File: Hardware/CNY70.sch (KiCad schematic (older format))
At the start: 3 parts

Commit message: Battery charger IC added
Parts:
- gave numbers to parts that had none: 3
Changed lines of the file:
@@
 Connection ~ 6250 4150
 $Comp
-L Sensor_Proximity:CNY70 U?
+L Sensor_Proximity:CNY70 U4
 U 1 1 5FEE7D3D
 P 5900 4050
-F 0 "U?" H 5900 4367 50  0000 C CNN
+AR Path="/5FEE7C2C/5FEE7D3D" Ref="U4"  Part="1"
+AR Path="/5FEFD023/5FEE7D3D" Ref="U7"  Part="1"
+F 0 "U7" H 5900 4367 50  0000 C CNN
 F 1 "CNY70" H 5900 4276 50  0000 C CNN
 F 2 "OptoDevice:Vishay_CNY70" H 5900 3850 50  0001 C CNN
@@
 $EndComp
 $Comp
-L Device:R_Small_US R?
+L Device:R_Small_US R19
 U 1 1 5FEE87CE
 P 5550 4300
-F 0 "R?" H 5618 4346 50  0000 L CNN
+AR Path="/5FEE7C2C/5FEE87CE" Ref="R19"  Part="1"
+AR Path="/5FEFD023/5FEE87CE" Ref="R21"  Part="1"
+F 0 "R21" H 5618 4346 50  0000 L CNN
 F 1 "80" H 5618 4255 50  0000 L CNN
 F 2 "" H 5550 4300 50  0001 C CNN
@@
 $EndComp
 $Comp
-L power:GND #PWR?
+L power:GND #PWR039
 U 1 1 5FEE941E
 P 5550 4400
-F 0 "#PWR?" H 5550 4150 50  0001 C CNN
+AR Path="/5FEE7C2C/5FEE941E" Ref="#PWR039"  Part="1"
+AR Path="/5FEFD023/5FEE941E" Ref="#PWR043"  Part="1"
+F 0 "#PWR043" H 5550 4150 50  0001 C CNN
 F 1 "GND" H 5555 4227 50  0000 C CNN
 F 2 "" H 5550 4400 50  0001 C CNN
@@
 $EndComp
 $Comp
-L power:+3.3V #PWR?
+L power:+3.3V #PWR037
 U 1 1 5FEFD560
 P 5550 3900
-F 0 "#PWR?" H 5550 3750 50  0001 C CNN
+AR Path="/5FEE7C2C/5FEFD560" Ref="#PWR037"  Part="1"
+AR Path="/5FEFD023/5FEFD560" Ref="#PWR041"  Part="1"
+F 0 "#PWR041" H 5550 3750 50  0001 C CNN
 F 1 "+3.3V" H 5565 4073 50  0000 C CNN
 F 2 "" H 5550 3900 50  0001 C CNN
@@
 $EndComp
 $Comp
-L power:+3.3V #PWR?
+L power:+3.3V #PWR038
 U 1 1 5FEFD561
 P 6250 3900
-F 0 "#PWR?" H 6250 3750 50  0001 C CNN
+AR Path="/5FEE7C2C/5FEFD561" Ref="#PWR038"  Part="1"
+AR Path="/5FEFD023/5FEFD561" Ref="#PWR042"  Part="1"
+F 0 "#PWR042" H 6250 3750 50  0001 C CNN
 F 1 "+3.3V" H 6265 4073 50  0000 C CNN
 F 2 "" H 6250 3900 50  0001 C CNN
@@
 $EndComp
 $Comp
-L Device:R_Small_US R?
+L Device:R_Small_US R20
 U 1 1 5FEFD562
 P 6250 4300
-F 0 "R?" H 6318 4346 50  0000 L CNN
+AR Path="/5FEE7C2C/5FEFD562" Ref="R20"  Part="1"
+AR Path="/5FEFD023/5FEFD562" Ref="R22"  Part="1"
+F 0 "R22" H 6318 4346 50  0000 L CNN
 F 1 "1k" H 6318 4255 50  0000 L CNN
 F 2 "" H 6250 4300 50  0001 C CNN
@@
 $EndComp
 $Comp
-L power:GND #PWR?
+L power:GND #PWR040
 U 1 1 5FEFD563
 P 6250 4400
-F 0 "#PWR?" H 6250 4150 50  0001 C CNN
+AR Path="/5FEE7C2C/5FEFD563" Ref="#PWR040"  Part="1"
+AR Path="/5FEFD023/5FEFD563" Ref="#PWR044"  Part="1"
+F 0 "#PWR044" H 6250 4150 50  0001 C CNN
 F 1 "GND" H 6255 4227 50  0000 C CNN
 F 2 "" H 6250 4400 50  0001 C CNN

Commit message: Replaced ESP-WROOM-32D with ESP32-CAM
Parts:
- added R?: 80, symbol Device:R_Small_US
- renumbered R20 to R10, R19 to R9, U4 to U3
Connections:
- net +3V3: now also R?.1; no longer U3.3 (C)
- new net: R?.2, U3.3 (C)
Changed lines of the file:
@@
 	5550 3950 5600 3950
 Wire Wire Line
-	6250 3900 6250 3950
+	6250 3700 6250 3750
 Wire Wire Line
 	6250 3950 6200 3950
@@
 Connection ~ 6250 4150
 $Comp
-L Sensor_Proximity:CNY70 U4
+L Sensor_Proximity:CNY70 U3
 U 1 1 5FEE7D3D
 P 5900 4050
-AR Path="/5FEE7C2C/5FEE7D3D" Ref="U4"  Part="1"
-AR Path="/5FEFD023/5FEE7D3D" Ref="U7"  Part="1"
-F 0 "U7" H 5900 4367 50  0000 C CNN
+AR Path="/5FEE7C2C/5FEE7D3D" Ref="U3"  Part="1"
+AR Path="/5FEFD023/5FEE7D3D" Ref="U4"  Part="1"
+F 0 "U3" H 5900 4367 50  0000 C CNN
 F 1 "CNY70" H 5900 4276 50  0000 C CNN
 F 2 "OptoDevice:Vishay_CNY70" H 5900 3850 50  0001 C CNN
@@
 $EndComp
 $Comp
-L Device:R_Small_US R19
+L Device:R_Small_US R9
 U 1 1 5FEE87CE
 P 5550 4300
-AR Path="/5FEE7C2C/5FEE87CE" Ref="R19"  Part="1"
-AR Path="/5FEFD023/5FEE87CE" Ref="R21"  Part="1"
-F 0 "R21" H 5618 4346 50  0000 L CNN
+AR Path="/5FEE7C2C/5FEE87CE" Ref="R9"  Part="1"
+AR Path="/5FEFD023/5FEE87CE" Ref="R11"  Part="1"
+F 0 "R9" H 5618 4346 50  0000 L CNN
 F 1 "80" H 5618 4255 50  0000 L CNN
 F 2 "" H 5550 4300 50  0001 C CNN
@@
 $EndComp
 $Comp
-L power:GND #PWR039
+L power:GND #PWR028
 U 1 1 5FEE941E
 P 5550 4400
-AR Path="/5FEE7C2C/5FEE941E" Ref="#PWR039"  Part="1"
-AR Path="/5FEFD023/5FEE941E" Ref="#PWR043"  Part="1"
-F 0 "#PWR043" H 5550 4150 50  0001 C CNN
+AR Path="/5FEE7C2C/5FEE941E" Ref="#PWR028"  Part="1"
+AR Path="/5FEFD023/5FEE941E" Ref="#PWR032"  Part="1"
+F 0 "#PWR028" H 5550 4150 50  0001 C CNN
 F 1 "GND" H 5555 4227 50  0000 C CNN
 F 2 "" H 5550 4400 50  0001 C CNN
@@
 $EndComp
 $Comp
-L power:+3.3V #PWR037
+L power:+3.3V #PWR026
 U 1 1 5FEFD560
 P 5550 3900
-AR Path="/5FEE7C2C/5FEFD560" Ref="#PWR037"  Part="1"
-AR Path="/5FEFD023/5FEFD560" Ref="#PWR041"  Part="1"
-F 0 "#PWR041" H 5550 3750 50  0001 C CNN
+AR Path="/5FEE7C2C/5FEFD560" Ref="#PWR026"  Part="1"
+AR Path="/5FEFD023/5FEFD560" Ref="#PWR030"  Part="1"
+F 0 "#PWR026" H 5550 3750 50  0001 C CNN
 F 1 "+3.3V" H 5565 4073 50  0000 C CNN
 F 2 "" H 5550 3900 50  0001 C CNN
@@
 $EndComp
 $Comp
-L power:+3.3V #PWR038
+L power:+3.3V #PWR027
 U 1 1 5FEFD561
-P 6250 3900
-AR Path="/5FEE7C2C/5FEFD561" Ref="#PWR038"  Part="1"
-AR Path="/5FEFD023/5FEFD561" Ref="#PWR042"  Part="1"
-F 0 "#PWR042" H 6250 3750 50  0001 C CNN
-F 1 "+3.3V" H 6265 4073 50  0000 C CNN
-F 2 "" H 6250 3900 50  0001 C CNN
-F 3 "" H 6250 3900 50  0001 C CNN
-	1    6250 3900
+P 6250 3700
+AR Path="/5FEE7C2C/5FEFD561" Ref="#PWR027"  Part="1"
+AR Path="/5FEFD023/5FEFD561" Ref="#PWR031"  Part="1"
+F 0 "#PWR027" H 6250 3550 50  0001 C CNN
+F 1 "+3.3V" H 6265 3873 50  0000 C CNN
+F 2 "" H 6250 3700 50  0001 C CNN
+F 3 "" H 6250 3700 50  0001 C CNN
+	1    6250 3700
 	1    0    0    -1
 $EndComp
 $Comp
-L Device:R_Small_US R20
+L Device:R_Small_US R10
 U 1 1 5FEFD562
 P 6250 4300
-AR Path="/5FEE7C2C/5FEFD562" Ref="R20"  Part="1"
-AR Path="/5FEFD023/5FEFD562" Ref="R22"  Part="1"
-F 0 "R22" H 6318 4346 50  0000 L CNN
+AR Path="/5FEE7C2C/5FEFD562" Ref="R10"  Part="1"
+AR Path="/5FEFD023/5FEFD562" Ref="R12"  Part="1"
+F 0 "R10" H 6318 4346 50  0000 L CNN
 F 1 "1k" H 6318 4255 50  0000 L CNN
 F 2 "" H 6250 4300 50  0001 C CNN
@@
 $EndComp
 $Comp
-L power:GND #PWR040
+L power:GND #PWR029
 U 1 1 5FEFD563
 P 6250 4400
-AR Path="/5FEE7C2C/5FEFD563" Ref="#PWR040"  Part="1"
-AR Path="/5FEFD023/5FEFD563" Ref="#PWR044"  Part="1"
-F 0 "#PWR044" H 6250 4150 50  0001 C CNN
+AR Path="/5FEE7C2C/5FEFD563" Ref="#PWR029"  Part="1"
+AR Path="/5FEFD023/5FEFD563" Ref="#PWR033"  Part="1"
+F 0 "#PWR029" H 6250 4150 50  0001 C CNN
 F 1 "GND" H 6255 4227 50  0000 C CNN
 F 2 "" H 6250 4400 50  0001 C CNN
@@
 Text HLabel 6300 4150 2    50   Output ~ 0
 IR
+$Comp
+L Device:R_Small_US R?
+U 1 1 5FF4EFE4
+P 6250 3850
+AR Path="/5FEE7C2C/5FF4EFE4" Ref="R?"  Part="1"
+AR Path="/5FEFD023/5FF4EFE4" Ref="R?"  Part="1"
+F 0 "R?" H 6318 3896 50  0000 L CNN
+F 1 "80" H 6318 3805 50  0000 L CNN
+F 2 "" H 6250 3850 50  0001 C CNN
+F 3 "~" H 6250 3850 50  0001 C CNN
+	1    6250 3850
+	1    0    0    -1
+$EndComp
 $EndSCHEMATC

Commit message: Signed-off-by: Usman <usmanmehmood55@gmail.com>
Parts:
- removed R?: 80, symbol Device:R_Small_US
- added R9: 80, symbol Device:R_Small_US
- renumbered R9 to R10, R10 to R11
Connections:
- net +3V3: now also U3.3 (C)
- net IR: now also R9.2; no longer R11.1, U3.4 (E)
- new net: R11.1, R9.1, U3.4 (E)
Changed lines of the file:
@@
 	5550 3950 5600 3950
 Wire Wire Line
-	6250 3700 6250 3750
+	6250 3900 6250 3950
 Wire Wire Line
 	6250 3950 6200 3950
@@
 $EndComp
 $Comp
-L Device:R_Small_US R9
+L Device:R_Small_US R10
 U 1 1 5FEE87CE
 P 5550 4300
-AR Path="/5FEE7C2C/5FEE87CE" Ref="R9"  Part="1"
-AR Path="/5FEFD023/5FEE87CE" Ref="R11"  Part="1"
-F 0 "R9" H 5618 4346 50  0000 L CNN
+AR Path="/5FEE7C2C/5FEE87CE" Ref="R10"  Part="1"
+AR Path="/5FEFD023/5FEE87CE" Ref="R13"  Part="1"
+F 0 "R10" H 5618 4346 50  0000 L CNN
 F 1 "80" H 5618 4255 50  0000 L CNN
 F 2 "" H 5550 4300 50  0001 C CNN
@@
 $EndComp
 $Comp
-L power:+3.3V #PWR026
+L power:+3.3V #PWR027
 U 1 1 5FEFD560
 P 5550 3900
-AR Path="/5FEE7C2C/5FEFD560" Ref="#PWR026"  Part="1"
-AR Path="/5FEFD023/5FEFD560" Ref="#PWR030"  Part="1"
-F 0 "#PWR026" H 5550 3750 50  0001 C CNN
+AR Path="/5FEE7C2C/5FEFD560" Ref="#PWR027"  Part="1"
+AR Path="/5FEFD023/5FEFD560" Ref="#PWR031"  Part="1"
+F 0 "#PWR027" H 5550 3750 50  0001 C CNN
 F 1 "+3.3V" H 5565 4073 50  0000 C CNN
 F 2 "" H 5550 3900 50  0001 C CNN
@@
 $EndComp
 $Comp
-L power:+3.3V #PWR027
+L power:+3.3V #PWR026
 U 1 1 5FEFD561
-P 6250 3700
-AR Path="/5FEE7C2C/5FEFD561" Ref="#PWR027"  Part="1"
-AR Path="/5FEFD023/5FEFD561" Ref="#PWR031"  Part="1"
-F 0 "#PWR027" H 6250 3550 50  0001 C CNN
-F 1 "+3.3V" H 6265 3873 50  0000 C CNN
-F 2 "" H 6250 3700 50  0001 C CNN
-F 3 "" H 6250 3700 50  0001 C CNN
-	1    6250 3700
+P 6250 3900
+AR Path="/5FEE7C2C/5FEFD561" Ref="#PWR026"  Part="1"
+AR Path="/5FEFD023/5FEFD561" Ref="#PWR030"  Part="1"
+F 0 "#PWR026" H 6250 3750 50  0001 C CNN
+F 1 "+3.3V" H 6265 4073 50  0000 C CNN
+F 2 "" H 6250 3900 50  0001 C CNN
+F 3 "" H 6250 3900 50  0001 C CNN
+	1    6250 3900
 	1    0    0    -1
 $EndComp
 $Comp
-L Device:R_Small_US R10
+L Device:R_Small_US R11
 U 1 1 5FEFD562
 P 6250 4300
-AR Path="/5FEE7C2C/5FEFD562" Ref="R10"  Part="1"
-AR Path="/5FEFD023/5FEFD562" Ref="R12"  Part="1"
-F 0 "R10" H 6318 4346 50  0000 L CNN
+AR Path="/5FEE7C2C/5FEFD562" Ref="R11"  Part="1"
+AR Path="/5FEFD023/5FEFD562" Ref="R14"  Part="1"
+F 0 "R11" H 6318 4346 50  0000 L CNN
 F 1 "1k" H 6318 4255 50  0000 L CNN
 F 2 "" H 6250 4300 50  0001 C CNN
@@
 	1    0    0    -1
 $EndComp
-Text HLabel 6300 4150 2    50   Output ~ 0
+Text HLabel 6500 4150 2    50   Output ~ 0
 IR
 $Comp
-L Device:R_Small_US R?
-U 1 1 5FF4EFE4
-P 6250 3850
-AR Path="/5FEE7C2C/5FF4EFE4" Ref="R?"  Part="1"
-AR Path="/5FEFD023/5FF4EFE4" Ref="R?"  Part="1"
-F 0 "R?" H 6318 3896 50  0000 L CNN
-F 1 "80" H 6318 3805 50  0000 L CNN
-F 2 "" H 6250 3850 50  0001 C CNN
-F 3 "~" H 6250 3850 50  0001 C CNN
-	1    6250 3850
-	1    0    0    -1
+L Device:R_Small_US R9
+U 1 1 60707AE9
+P 6400 4150
+AR Path="/5FEE7C2C/60707AE9" Ref="R9"  Part="1"
+AR Path="/5FEFD023/60707AE9" Ref="R12"  Part="1"
+F 0 "R9" V 6600 4100 50  0000 L CNN
+F 1 "80" V 6500 4100 50  0000 L CNN
+F 2 "" H 6400 4150 50  0001 C CNN
+F 3 "~" H 6400 4150 50  0001 C CNN
+	1    6400 4150
+	0    -1   -1   0
 $EndComp
 $EndSCHEMATC

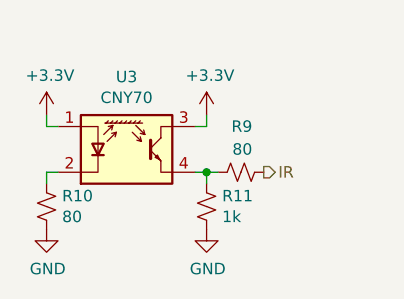
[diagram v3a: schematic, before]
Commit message: Schematic updated, USB comms circuit added
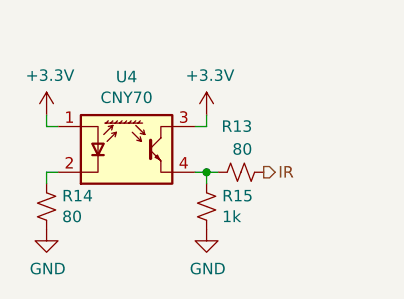
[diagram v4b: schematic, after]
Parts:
- R13: renamed from R9; footprint (none) -> Resistor_SMD:R_0805_2012Metric
- R14: renamed from R10; footprint (none) -> Resistor_SMD:R_0805_2012Metric
- R15: renamed from R11; footprint (none) -> Resistor_SMD:R_0805_2012Metric
- renumbered U3 to U4
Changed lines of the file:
@@
 $Descr A4 11693 8268
 encoding utf-8
-Sheet 4 9
+Sheet 4 11
 Title ""
 Date ""
@@
 Connection ~ 6250 4150
 $Comp
-L Sensor_Proximity:CNY70 U3
+L Sensor_Proximity:CNY70 U4
 U 1 1 5FEE7D3D
 P 5900 4050
-AR Path="/5FEE7C2C/5FEE7D3D" Ref="U3"  Part="1"
-AR Path="/5FEFD023/5FEE7D3D" Ref="U4"  Part="1"
-F 0 "U3" H 5900 4367 50  0000 C CNN
+AR Path="/5FEE7C2C/5FEE7D3D" Ref="U4"  Part="1"
+AR Path="/5FEFD023/5FEE7D3D" Ref="U5"  Part="1"
+F 0 "U4" H 5900 4367 50  0000 C CNN
 F 1 "CNY70" H 5900 4276 50  0000 C CNN
 F 2 "OptoDevice:Vishay_CNY70" H 5900 3850 50  0001 C CNN
@@
 $EndComp
 $Comp
-L Device:R_Small_US R10
+L Device:R_Small_US R14
 U 1 1 5FEE87CE
 P 5550 4300
-AR Path="/5FEE7C2C/5FEE87CE" Ref="R10"  Part="1"
-AR Path="/5FEFD023/5FEE87CE" Ref="R13"  Part="1"
-F 0 "R10" H 5618 4346 50  0000 L CNN
+AR Path="/5FEE7C2C/5FEE87CE" Ref="R14"  Part="1"
+AR Path="/5FEFD023/5FEE87CE" Ref="R17"  Part="1"
+F 0 "R14" H 5618 4346 50  0000 L CNN
 F 1 "80" H 5618 4255 50  0000 L CNN
-F 2 "" H 5550 4300 50  0001 C CNN
+F 2 "Resistor_SMD:R_0805_2012Metric" H 5550 4300 50  0001 C CNN
 F 3 "~" H 5550 4300 50  0001 C CNN
 	1    5550 4300
@@
 $EndComp
 $Comp
-L power:GND #PWR028
+L power:GND #PWR032
 U 1 1 5FEE941E
 P 5550 4400
-AR Path="/5FEE7C2C/5FEE941E" Ref="#PWR028"  Part="1"
-AR Path="/5FEFD023/5FEE941E" Ref="#PWR032"  Part="1"
-F 0 "#PWR028" H 5550 4150 50  0001 C CNN
+AR Path="/5FEE7C2C/5FEE941E" Ref="#PWR032"  Part="1"
+AR Path="/5FEFD023/5FEE941E" Ref="#PWR036"  Part="1"
+F 0 "#PWR036" H 5550 4150 50  0001 C CNN
 F 1 "GND" H 5555 4227 50  0000 C CNN
 F 2 "" H 5550 4400 50  0001 C CNN
@@
 $EndComp
 $Comp
-L power:+3.3V #PWR027
+L power:+3.3V #PWR030
 U 1 1 5FEFD560
 P 5550 3900
-AR Path="/5FEE7C2C/5FEFD560" Ref="#PWR027"  Part="1"
-AR Path="/5FEFD023/5FEFD560" Ref="#PWR031"  Part="1"
-F 0 "#PWR027" H 5550 3750 50  0001 C CNN
+AR Path="/5FEE7C2C/5FEFD560" Ref="#PWR030"  Part="1"
+AR Path="/5FEFD023/5FEFD560" Ref="#PWR034"  Part="1"
+F 0 "#PWR034" H 5550 3750 50  0001 C CNN
 F 1 "+3.3V" H 5565 4073 50  0000 C CNN
 F 2 "" H 5550 3900 50  0001 C CNN
@@
 $EndComp
 $Comp
-L power:+3.3V #PWR026
+L power:+3.3V #PWR031
 U 1 1 5FEFD561
 P 6250 3900
-AR Path="/5FEE7C2C/5FEFD561" Ref="#PWR026"  Part="1"
-AR Path="/5FEFD023/5FEFD561" Ref="#PWR030"  Part="1"
-F 0 "#PWR026" H 6250 3750 50  0001 C CNN
+AR Path="/5FEE7C2C/5FEFD561" Ref="#PWR031"  Part="1"
+AR Path="/5FEFD023/5FEFD561" Ref="#PWR035"  Part="1"
+F 0 "#PWR035" H 6250 3750 50  0001 C CNN
 F 1 "+3.3V" H 6265 4073 50  0000 C CNN
 F 2 "" H 6250 3900 50  0001 C CNN
@@
 $EndComp
 $Comp
-L Device:R_Small_US R11
+L Device:R_Small_US R15
 U 1 1 5FEFD562
 P 6250 4300
-AR Path="/5FEE7C2C/5FEFD562" Ref="R11"  Part="1"
-AR Path="/5FEFD023/5FEFD562" Ref="R14"  Part="1"
-F 0 "R11" H 6318 4346 50  0000 L CNN
+AR Path="/5FEE7C2C/5FEFD562" Ref="R15"  Part="1"
+AR Path="/5FEFD023/5FEFD562" Ref="R18"  Part="1"
+F 0 "R15" H 6318 4346 50  0000 L CNN
 F 1 "1k" H 6318 4255 50  0000 L CNN
-F 2 "" H 6250 4300 50  0001 C CNN
+F 2 "Resistor_SMD:R_0805_2012Metric" H 6250 4300 50  0001 C CNN
 F 3 "~" H 6250 4300 50  0001 C CNN
 	1    6250 4300
@@
 $EndComp
 $Comp
-L power:GND #PWR029
+L power:GND #PWR033
 U 1 1 5FEFD563
 P 6250 4400
-AR Path="/5FEE7C2C/5FEFD563" Ref="#PWR029"  Part="1"
-AR Path="/5FEFD023/5FEFD563" Ref="#PWR033"  Part="1"
-F 0 "#PWR029" H 6250 4150 50  0001 C CNN
+AR Path="/5FEE7C2C/5FEFD563" Ref="#PWR033"  Part="1"
+AR Path="/5FEFD023/5FEFD563" Ref="#PWR037"  Part="1"
+F 0 "#PWR037" H 6250 4150 50  0001 C CNN
 F 1 "GND" H 6255 4227 50  0000 C CNN
 F 2 "" H 6250 4400 50  0001 C CNN
@@
 IR
 $Comp
-L Device:R_Small_US R9
+L Device:R_Small_US R13
 U 1 1 60707AE9
 P 6400 4150
-AR Path="/5FEE7C2C/60707AE9" Ref="R9"  Part="1"
-AR Path="/5FEFD023/60707AE9" Ref="R12"  Part="1"
-F 0 "R9" V 6600 4100 50  0000 L CNN
+AR Path="/5FEE7C2C/60707AE9" Ref="R13"  Part="1"
+AR Path="/5FEFD023/60707AE9" Ref="R16"  Part="1"
+F 0 "R13" V 6600 4100 50  0000 L CNN
 F 1 "80" V 6500 4100 50  0000 L CNN
-F 2 "" H 6400 4150 50  0001 C CNN
+F 2 "Resistor_SMD:R_0805_2012Metric" H 6400 4150 50  0001 C CNN
 F 3 "~" H 6400 4150 50  0001 C CNN
 	1    6400 4150

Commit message: PCB design started
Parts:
- added R21: 50R, Resistor_SMD:R_0805_2012Metric, symbol Roverette-rescue:R_Small_US-Device
- R13: renamed from R14; symbol Device:R_Small_US -> Roverette-rescue:R_Small_US-Device
- R14: renamed from R15; symbol Device:R_Small_US -> Roverette-rescue:R_Small_US-Device
- R15: renamed from R13; symbol Device:R_Small_US -> Roverette-rescue:R_Small_US-Device
- U3: renamed from U4; symbol Sensor_Proximity:CNY70 -> Roverette-rescue:CNY70-Sensor_Proximity
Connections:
- net +3V3: now also R21.1; no longer U3.3 (C)
- new net: R21.2, U3.3 (C)
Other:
- moved on the sheet: R18
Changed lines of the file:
@@
 $Descr A4 11693 8268
 encoding utf-8
-Sheet 4 12
+Sheet 4 11
 Title ""
 Date ""
@@
 Wire Wire Line
 	6250 4150 6200 4150
-Wire Wire Line
-	6300 4150 6250 4150
 Connection ~ 6250 4150
 $Comp
-L Sensor_Proximity:CNY70 U4
+L Roverette-rescue:CNY70-Sensor_Proximity U3
 U 1 1 5FEE7D3D
 P 5900 4050
-AR Path="/5FEE7C2C/5FEE7D3D" Ref="U4"  Part="1"
-AR Path="/5FEFD023/5FEE7D3D" Ref="U5"  Part="1"
+AR Path="/5FEE7C2C/5FEE7D3D" Ref="U3"  Part="1"
+AR Path="/5FEFD023/5FEE7D3D" Ref="U4"  Part="1"
 F 0 "U4" H 5900 4367 50  0000 C CNN
 F 1 "CNY70" H 5900 4276 50  0000 C CNN
@@
 $EndComp
 $Comp
-L Device:R_Small_US R14
+L Roverette-rescue:R_Small_US-Device R13
 U 1 1 5FEE87CE
 P 5550 4300
-AR Path="/5FEE7C2C/5FEE87CE" Ref="R14"  Part="1"
-AR Path="/5FEFD023/5FEE87CE" Ref="R17"  Part="1"
-F 0 "R14" H 5618 4346 50  0000 L CNN
+AR Path="/5FEE7C2C/5FEE87CE" Ref="R13"  Part="1"
+AR Path="/5FEFD023/5FEE87CE" Ref="R16"  Part="1"
+F 0 "R16" H 5618 4346 50  0000 L CNN
 F 1 "80" H 5618 4255 50  0000 L CNN
 F 2 "Resistor_SMD:R_0805_2012Metric" H 5550 4300 50  0001 C CNN
@@
 $EndComp
 $Comp
-L power:GND #PWR032
+L Roverette-rescue:GND-power #PWR029
 U 1 1 5FEE941E
 P 5550 4400
-AR Path="/5FEE7C2C/5FEE941E" Ref="#PWR032"  Part="1"
-AR Path="/5FEFD023/5FEE941E" Ref="#PWR036"  Part="1"
-F 0 "#PWR036" H 5550 4150 50  0001 C CNN
+AR Path="/5FEE7C2C/5FEE941E" Ref="#PWR029"  Part="1"
+AR Path="/5FEFD023/5FEE941E" Ref="#PWR033"  Part="1"
+F 0 "#PWR033" H 5550 4150 50  0001 C CNN
 F 1 "GND" H 5555 4227 50  0000 C CNN
 F 2 "" H 5550 4400 50  0001 C CNN
@@
 $EndComp
 $Comp
-L power:+3.3V #PWR030
+L Roverette-rescue:+3.3V-power #PWR028
 U 1 1 5FEFD560
 P 5550 3900
-AR Path="/5FEE7C2C/5FEFD560" Ref="#PWR030"  Part="1"
-AR Path="/5FEFD023/5FEFD560" Ref="#PWR034"  Part="1"
-F 0 "#PWR034" H 5550 3750 50  0001 C CNN
+AR Path="/5FEE7C2C/5FEFD560" Ref="#PWR028"  Part="1"
+AR Path="/5FEFD023/5FEFD560" Ref="#PWR032"  Part="1"
+F 0 "#PWR032" H 5550 3750 50  0001 C CNN
 F 1 "+3.3V" H 5565 4073 50  0000 C CNN
 F 2 "" H 5550 3900 50  0001 C CNN
@@
 $EndComp
 $Comp
-L power:+3.3V #PWR031
+L Roverette-rescue:+3.3V-power #PWR030
 U 1 1 5FEFD561
-P 6250 3900
-AR Path="/5FEE7C2C/5FEFD561" Ref="#PWR031"  Part="1"
-AR Path="/5FEFD023/5FEFD561" Ref="#PWR035"  Part="1"
-F 0 "#PWR035" H 6250 3750 50  0001 C CNN
-F 1 "+3.3V" H 6265 4073 50  0000 C CNN
-F 2 "" H 6250 3900 50  0001 C CNN
-F 3 "" H 6250 3900 50  0001 C CNN
-	1    6250 3900
+P 6250 3700
+AR Path="/5FEE7C2C/5FEFD561" Ref="#PWR030"  Part="1"
+AR Path="/5FEFD023/5FEFD561" Ref="#PWR034"  Part="1"
+F 0 "#PWR034" H 6250 3550 50  0001 C CNN
+F 1 "+3.3V" H 6265 3873 50  0000 C CNN
+F 2 "" H 6250 3700 50  0001 C CNN
+F 3 "" H 6250 3700 50  0001 C CNN
+	1    6250 3700
 	1    0    0    -1
 $EndComp
 $Comp
-L Device:R_Small_US R15
+L Roverette-rescue:R_Small_US-Device R14
 U 1 1 5FEFD562
 P 6250 4300
-AR Path="/5FEE7C2C/5FEFD562" Ref="R15"  Part="1"
-AR Path="/5FEFD023/5FEFD562" Ref="R18"  Part="1"
-F 0 "R15" H 6318 4346 50  0000 L CNN
+AR Path="/5FEE7C2C/5FEFD562" Ref="R14"  Part="1"
+AR Path="/5FEFD023/5FEFD562" Ref="R17"  Part="1"
+F 0 "R17" H 6318 4346 50  0000 L CNN
 F 1 "1k" H 6318 4255 50  0000 L CNN
 F 2 "Resistor_SMD:R_0805_2012Metric" H 6250 4300 50  0001 C CNN
@@
 $EndComp
 $Comp
-L power:GND #PWR033
+L Roverette-rescue:GND-power #PWR031
 U 1 1 5FEFD563
 P 6250 4400
-AR Path="/5FEE7C2C/5FEFD563" Ref="#PWR033"  Part="1"
-AR Path="/5FEFD023/5FEFD563" Ref="#PWR037"  Part="1"
-F 0 "#PWR037" H 6250 4150 50  0001 C CNN
+AR Path="/5FEE7C2C/5FEFD563" Ref="#PWR031"  Part="1"
+AR Path="/5FEFD023/5FEFD563" Ref="#PWR035"  Part="1"
+F 0 "#PWR035" H 6250 4150 50  0001 C CNN
 F 1 "GND" H 6255 4227 50  0000 C CNN
 F 2 "" H 6250 4400 50  0001 C CNN
@@
 	1    0    0    -1
 $EndComp
-Text HLabel 6500 4150 2    50   Output ~ 0
+Text HLabel 6850 4150 2    50   Output ~ 0
 IR
 $Comp
-L Device:R_Small_US R13
+L Roverette-rescue:R_Small_US-Device R15
 U 1 1 60707AE9
-P 6400 4150
-AR Path="/5FEE7C2C/60707AE9" Ref="R13"  Part="1"
-AR Path="/5FEFD023/60707AE9" Ref="R16"  Part="1"
-F 0 "R13" V 6600 4100 50  0000 L CNN
-F 1 "80" V 6500 4100 50  0000 L CNN
-F 2 "Resistor_SMD:R_0805_2012Metric" H 6400 4150 50  0001 C CNN
-F 3 "~" H 6400 4150 50  0001 C CNN
-	1    6400 4150
+P 6750 4150
+AR Path="/5FEE7C2C/60707AE9" Ref="R15"  Part="1"
+AR Path="/5FEFD023/60707AE9" Ref="R18"  Part="1"
+F 0 "R18" V 6950 4100 50  0000 L CNN
+F 1 "80" V 6850 4100 50  0000 L CNN
+F 2 "Resistor_SMD:R_0805_2012Metric" H 6750 4150 50  0001 C CNN
+F 3 "~" H 6750 4150 50  0001 C CNN
+	1    6750 4150
 	0    -1   -1   0
 $EndComp
+$Comp
+L Roverette-rescue:R_Small_US-Device R21
+U 1 1 6317B212
+P 6250 3800
+AR Path="/5FEE7C2C/6317B212" Ref="R21"  Part="1"
+AR Path="/5FEFD023/6317B212" Ref="R22"  Part="1"
+F 0 "R22" H 6318 3846 50  0000 L CNN
+F 1 "50R" H 6318 3755 50  0000 L CNN
+F 2 "Resistor_SMD:R_0805_2012Metric" H 6250 3800 50  0001 C CNN
+F 3 "~" H 6250 3800 50  0001 C CNN
+	1    6250 3800
+	1    0    0    -1
+$EndComp
+Wire Wire Line
+	6250 4150 6650 4150
 $EndSCHEMATC
